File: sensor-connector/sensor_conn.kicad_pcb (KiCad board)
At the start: 2 copper layers, 44.8 x 40.5 mm, 11 parts, among them J1 SPS30 RS232, J2 SPS30 TTL, U1 MAX232A

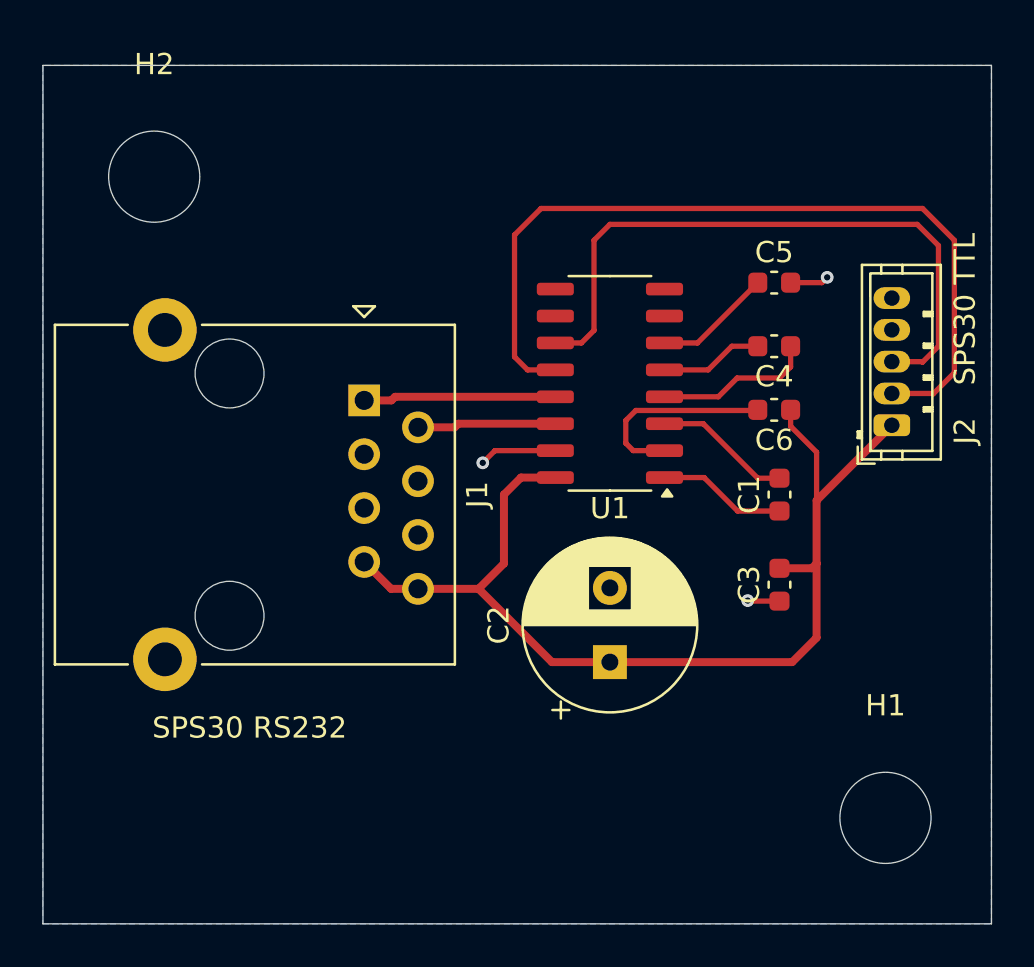
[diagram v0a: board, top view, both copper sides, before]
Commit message: changed mounting holes
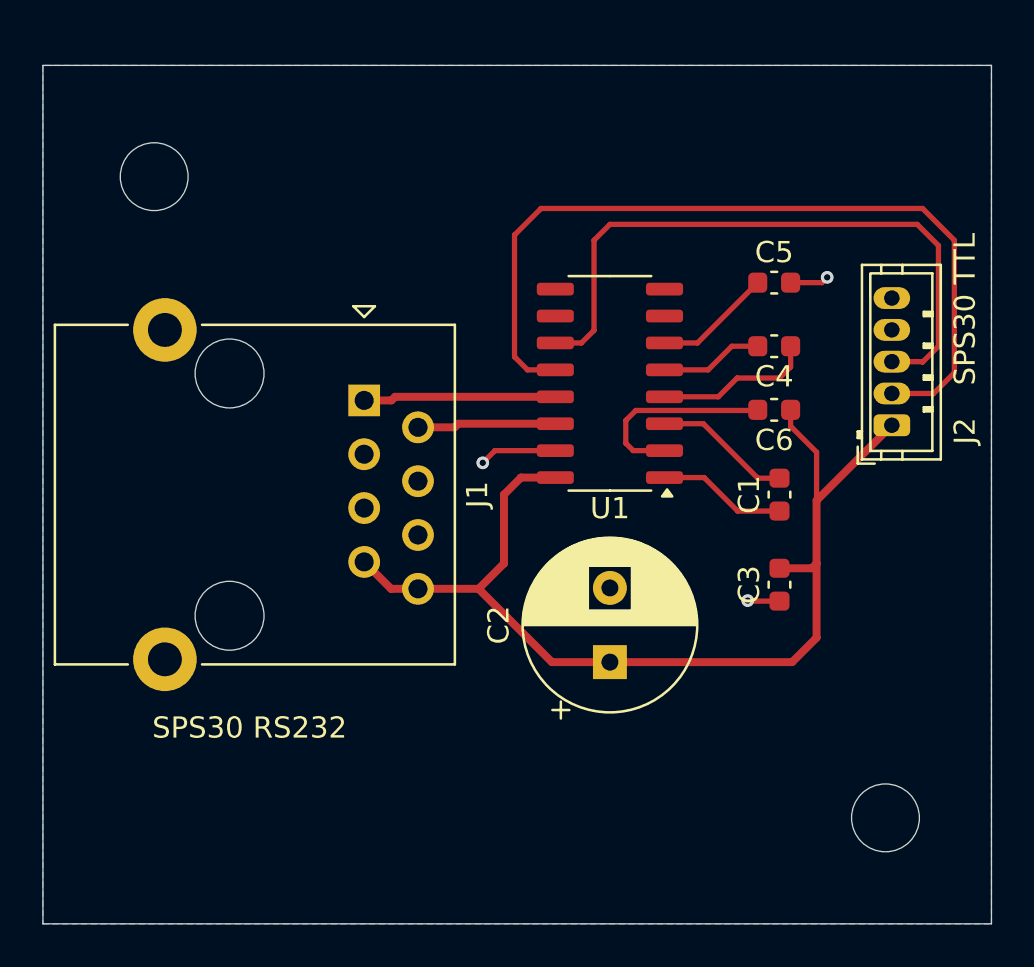
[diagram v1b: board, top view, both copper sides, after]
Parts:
- removed H1, H2: MountingHole, MountingHole:MountingHole_4.3mm_M4
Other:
- outline, holes or cut-outs redrawn
